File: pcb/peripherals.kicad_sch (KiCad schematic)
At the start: 24 parts, among them J2 Conn_01x24_MountingPin, J3 Conn_02x10_Odd_Even, U4 TLV74328PDBVR, U5 NRF24L01_Breakout, U6 TLV74315PDBVR, U7 BMI270

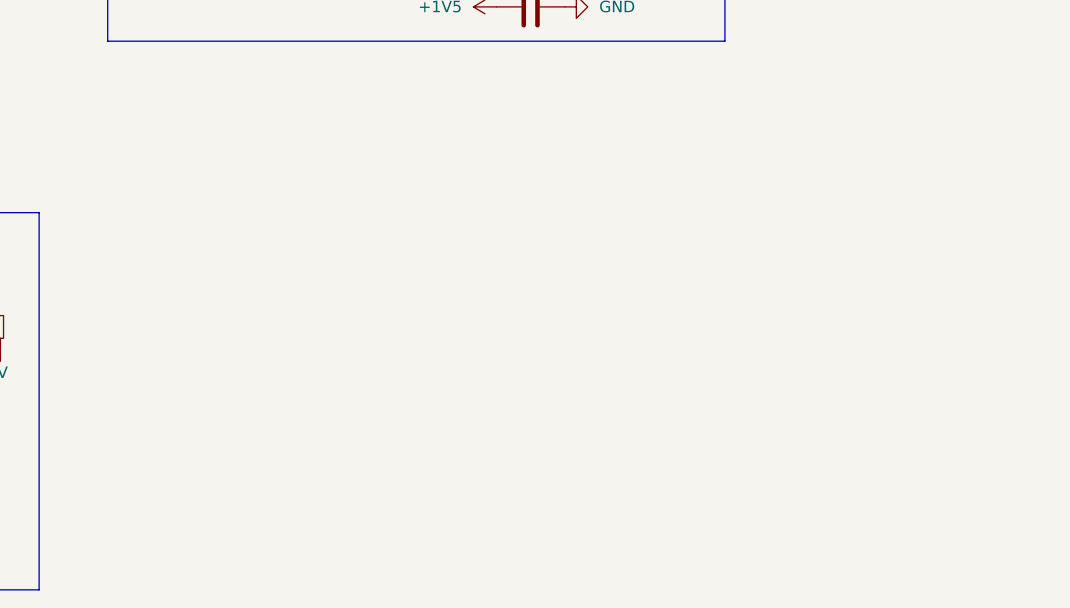
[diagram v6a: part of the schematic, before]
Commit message: [pcb] and [bom] add micro secure digital card interface socket connector
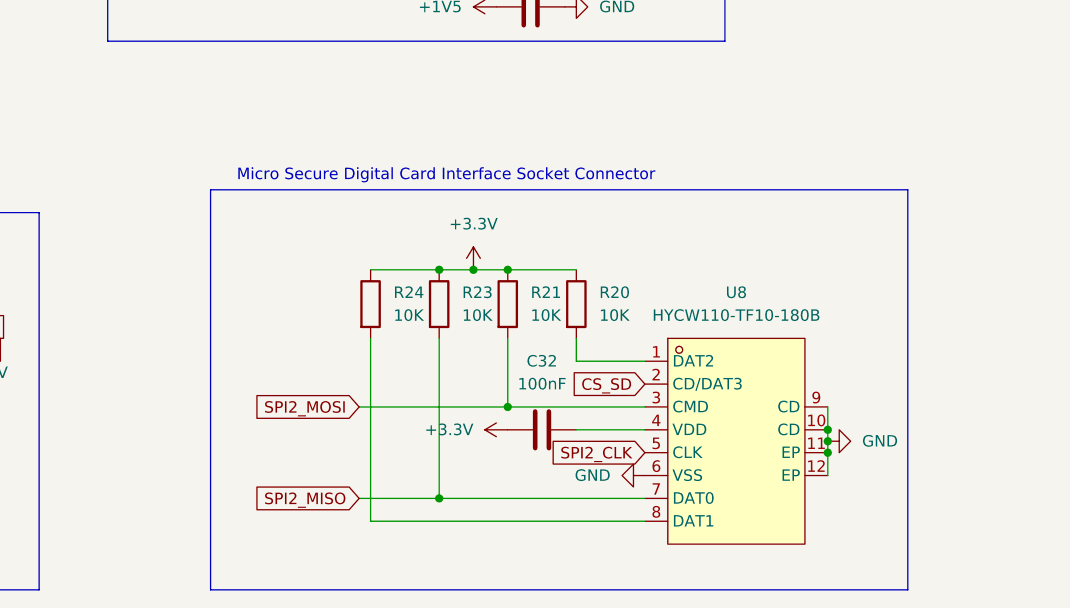
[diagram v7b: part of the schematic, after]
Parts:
- added C32: 100nF, symbol Device:C
- added R20, R21, R23, R24: 10K, symbol Device:R
- added U8: HYCW110-TF10-180B, lcsc:SIM-SMD_HYCW110-TF10-180B, symbol lcsc:HYCW110-TF10-180B
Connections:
- net +3.3V: now also C32.1, R20.1, R21.1, R23.1, R24.1
- net GND: now also U8.10 (CD), U8.11 (EP), U8.12 (EP), U8.6 (VSS), U8.9 (CD)
- net SPI2_CLK: now also U8.5 (CLK)
- net SPI2_MISO: now also R23.2, U8.7 (DAT0)
- net SPI2_MOSI: now also R21.2, U8.3 (CMD)
- new net: R20.2, U8.1 (DAT2)
- new net: C32.2, U8.4 (VDD)
- new net: R24.2, U8.8 (DAT1)
- new net CS_SD: U8.2 (CD/DAT3)
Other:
- note added: "Micro Secure Digital Card Interface Socket Connector"

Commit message: [pcb] continue routing - motors, camera, battery
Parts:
- C32: footprint (none) -> Capacitor_SMD:C_0805_2012Metric_Pad1.18x1.45mm_HandSolder; now not fitted
- R20, R21, R23, R24: value 10K -> 10k; footprint (none) -> Resistor_SMD:R_0805_2012Metric_Pad1.20x1.40mm_HandSolder
- U7: footprint lcsc:LGA-14_L3.0-W2.5-P0.50-BR -> Package_LGA:Bosch_LGA-14_3x2.5mm_P0.5mm
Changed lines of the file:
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@@
 			)
 		)
-		(property "Footprint" "lcsc:LGA-14_L3.0-W2.5-P0.50-BR"
+		(property "Footprint" "Package_LGA:Bosch_LGA-14_3x2.5mm_P0.5mm"
 			(at 43.18 148.59 0)
 			(effects
@@
 			)
 		)
-		(property "Value" "10K"
+		(property "Value" "10k"
 			(at 114.3 124.4599 0)
 			(effects
@@
 			)
 		)
-		(property "Footprint" ""
+		(property "Footprint" "Resistor_SMD:R_0805_2012Metric_Pad1.20x1.40mm_HandSolder"
 			(at 109.982 123.19 90)
 			(effects
@@
 			)
 		)
-		(property "Value" "10K"
+		(property "Value" "10k"
 			(at 137.16 124.4599 0)
 			(effects
@@
 			)
 		)
-		(property "Footprint" ""
+		(property "Footprint" "Resistor_SMD:R_0805_2012Metric_Pad1.20x1.40mm_HandSolder"
 			(at 132.842 123.19 90)
 			(effects
@@
 			)
 		)
-		(property "Value" "10K"
+		(property "Value" "10k"
 			(at 129.54 124.4599 0)
 			(effects
@@
 			)
 		)
-		(property "Footprint" ""
+		(property "Footprint" "Resistor_SMD:R_0805_2012Metric_Pad1.20x1.40mm_HandSolder"
 			(at 125.222 123.19 90)
 			(effects
@@
 		(in_bom yes)
 		(on_board yes)
-		(dnp no)
+		(dnp yes)
 		(property "Reference" "C32"
 			(at 130.81 129.54 90)
@@
 			)
 		)
-		(property "Footprint" ""
+		(property "Footprint" "Capacitor_SMD:C_0805_2012Metric_Pad1.18x1.45mm_HandSolder"
 			(at 134.62 136.1948 0)
 			(effects
@@
 			)
 		)
-		(property "Value" "10K"
+		(property "Value" "10k"
 			(at 121.92 124.4599 0)
 			(effects
@@
 			)
 		)
-		(property "Footprint" ""
+		(property "Footprint" "Resistor_SMD:R_0805_2012Metric_Pad1.20x1.40mm_HandSolder"
 			(at 117.602 123.19 90)
 			(effects
